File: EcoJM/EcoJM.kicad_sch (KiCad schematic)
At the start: 0 parts

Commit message: bahr updoad
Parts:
- added C1: 1n, symbol Device:C
- added C2, C4, C5: 100n, symbol Device:C
- added C3: 4.7n, symbol Device:C
- added R1: 10k, symbol Device:R
- added U1, U2: ACS712xLCTR-30A, Package_SO:SOIC-8_3.9x4.9mm_P1.27mm, symbol Sensor_Current:ACS712xLCTR-30A
- added U3: SIT65HVD230DR, EasyEDA:SOP-8_L4.9-W3.9-P1.27-LS6.0-BL, symbol EasyEDA:SIT65HVD230DR
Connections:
- new net: R1.1, U3.8 (RS)
- new net: C1.1, U1.6 (FILTER)
- new net: C3.1, U2.6 (FILTER)
- new net: U2.1 (IP+), U2.2 (IP+)
- new net: U2.3 (IP-), U2.4 (IP-)
- new net: U1.1 (IP+), U1.2 (IP+)
- new net: U1.3 (IP-), U1.4 (IP-)
- new net +3.3V: C5.2, U3.3 (VCC)
- new net +5V: C2.2, C4.2, U1.8 (VCC), U2.8 (VCC)
- new net GND: C1.2, C2.1, C3.2, C4.1, C5.1, R1.2, U1.5 (GND), U2.5 (GND), U3.2 (GND)

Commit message: Signed-off-by: Omar-Magdy0 <omar.magdy.om.om@gmail.com> Major Updates
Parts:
- removed U2: ACS712xLCTR-30A, Package_SO:SOIC-8_3.9x4.9mm_P1.27mm, symbol Sensor_Current:ACS712xLCTR-30A
- added C6: 22n, symbol Device:C
- added C7: 10u, symbol Device:C
- added F1: Fuse, Fuse:Fuseholder_Clip-5x20mm_Keystone_3512_Inline_P23.62x7.27mm_D1.02x1.57mm_Horizontal, symbol Device:Fuse
- added J1, J2: Screw_Terminal_01x02, symbol Connector:Screw_Terminal_01x02
- added J3, J4, J6: Conn_01x02_Pin, symbol Connector:Conn_01x02_Pin
- added J5, J7: Conn_01x03_Pin, symbol Connector:Conn_01x03_Pin
- added L1: 10u, symbol Device:L
- added R2, R6: 10k, symbol Device:R
- added R3, R4: R, symbol Device:R
- added R5: 120, symbol Device:R
- added R7: 20k, symbol Device:R
- added U2: MT2492, EasyEDA:SOT-23-6_L2.9-W1.6-P0.95-LS2.8-BL_3, symbol EasyEDA:MT2492
- added U4: AZ1117-3.3, Package_TO_SOT_SMD:SOT-89-3_Handsoldering, symbol Regulator_Linear:AZ1117-3.3
- added U5: RS321BXF, EasyEDA:SOT-23-5_L2.9-W1.6-P0.95-LS2.8-BL, symbol EasyEDA:RS321BXF
- C1: value 1n -> 4.7n
- C3: value 4.7n -> 22u
- C4: value 100n -> 22u
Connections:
- net +3.3V: now also C7.1, U4.2 (VO)
- net +5V: now also C3.2, L1.2, R3.1, U4.3 (VI); no longer C4.2
- net GND: now also C3.1, C4.2, C7.2, J3.2 (Pin_2), J4.2 (Pin_2), J5.3 (Pin_3), J7.3 (Pin_3), R4.2, R7.2, U2.2 (GND), U4.1 (GND); no longer C3.2, C4.1
- net CAN_TXD: now reaches U3.1 (D)
- net CAN_RXD: now reaches U3.4 (R)
- net CAN_L: now reaches U3.6 (CANL)
- net CAN_L: now also J5.2 (Pin_2), J6.2 (Pin_2)
- net CAN_H: now reaches U3.7 (CANH)
- net CAN_H: now also J5.1 (Pin_1), R5.1
- net at U1.1 (IP+), U1.2 (IP+): now also F1.2
- net VDCH+_OUT: now reaches U1.3 (IP-), U1.4 (IP-)
- net VDCH+_OUT: now also J2.1 (Pin_1)
- net at U1.7 (VIOUT): now also R6.1
- new net: C6.2, L1.1, U2.6 (SW)
- new net: J6.1 (Pin_1), R5.2
- new net: J4.1 (Pin_1), R2.1, U2.4 (EN)
- new net: R3.2, R4.1, U2.3 (FB)
- new net: C6.1, U2.1 (BS)
- new net +12V: C4.1, J3.1 (Pin_1), R2.2, U2.5 (IN)
- new net Current_M: R6.2, R7.1
- new net UART_RX: J7.2 (Pin_2)
- new net UART_TX: J7.1 (Pin_1)
- new net VDCH+_IN: F1.1, J1.1 (Pin_1)
- new net VDCH-: J1.2 (Pin_2), J2.2 (Pin_2)
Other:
- moved on the sheet: C1, C2, C5, R1, U1, U3

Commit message: sry forgot to save schematic xD
sry forgot to save schematic xD
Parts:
- added U6: STM32F_dev, symbol STM32F_devboard:STM32F_Bluepill
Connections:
- net CAN_RXD: now also U6.16 (B8)
- net CAN_TXD: now also U6.17 (B9)
- net UART_RX: now also U6.15 (B7)
- net UART_TX: now also U6.14 (B6)
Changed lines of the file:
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@@
 	(wire
 		(pts
+			(xy 27.94 97.79) (xy 36.83 97.79)
+		)
+		(stroke
+			(width 0)
+			(type default)
+		)
+	)
+	(wire
+		(pts
 			(xy 152.4 27.94) (xy 152.4 25.4)
 		)
@@
 	(wire
 		(pts
+			(xy 27.94 93.98) (xy 36.83 93.98)
+		)
+		(stroke
+			(width 0)
+			(type default)
+		)
+	)
+	(wire
+		(pts
 			(xy 147.32 166.37) (xy 147.32 170.18)
 		)
@@
 	(wire
 		(pts
+			(xy 27.94 101.6) (xy 36.83 101.6)
+		)
+		(stroke
+			(width 0)
+			(type default)
+		)
+	)
+	(wire
+		(pts
 			(xy 134.62 177.8) (xy 134.62 180.34)
 		)
@@
 	(wire
 		(pts
+			(xy 27.94 105.41) (xy 36.83 105.41)
+		)
+		(stroke
+			(width 0)
+			(type default)
+		)
+	)
+	(wire
+		(pts
 			(xy 63.5 170.18) (xy 60.96 170.18)
 		)
@@
 		)
 	)
+	(label "CAN_RXD"
+		(at 27.94 101.6 0)
+		(effects
+			(font
+				(size 1.27 1.27)
+			)
+			(justify left bottom)
+		)
+	)
 	(label "VDCH-"
 		(at 231.14 135.89 180)
@@
 		)
 	)
+	(label "CAN_TXD"
+		(at 27.94 105.41 0)
+		(effects
+			(font
+				(size 1.27 1.27)
+			)
+			(justify left bottom)
+		)
+	)
+	(label "UART_RX"
+		(at 27.94 97.79 180)
+		(effects
+			(font
+				(size 1.27 1.27)
+			)
+			(justify right bottom)
+		)
+	)
+	(label "UART_TX"
+		(at 27.94 93.98 180)
+		(effects
+			(font
+				(size 1.27 1.27)
+			)
+			(justify right bottom)
+		)
+	)
 	(symbol
 		(lib_id "power:GND")
@@
 	)
 	(symbol
+		(lib_id "STM32F_devboard:STM32F_Bluepill")
+		(at 54.61 50.8 0)
+		(unit 1)
+		(exclude_from_sim no)
+		(in_bom yes)
+		(on_board yes)
+		(dnp no)
+		(fields_autoplaced yes)
+		(property "Reference" "U6"
+			(at 54.61 38.1 0)
+			(effects
+				(font
+					(size 1.27 1.27)
+				)
+			)
+		)
+		(property "Value" "STM32F_dev"
+			(at 54.61 40.64 0)
+			(effects
+				(font
+					(size 1.27 1.27)
+				)
+			)
+		)
+		(property "Footprint" ""
+			(at 54.61 50.8 0)
+			(effects
+				(font
+					(size 1.27 1.27)
+				)
+				(hide yes)
+			)
+		)
+		(property "Datasheet" ""
+			(at 54.61 50.8 0)
+			(effects
+				(font
+					(size 1.27 1.27)
+				)
+				(hide yes)
+			)
+		)
+		(property "Description" ""
+			(at 54.61 50.8 0)
+			(effects
+				(font
+					(size 1.27 1.27)
+				)
+				(hide yes)
+			)
+		)
+		(pin "14"
+		)
+		(pin "25"
+		)
+		(pin "1"
+		)
+		(pin "11"
+		)
+		(pin "15"
+		)
+		(pin "17"
+		)
+		(pin "19"
+		)
+		(pin "12"
+		)
+		(pin "24"
+		)
+		(pin "13"
+		)
+		(pin "18"
+		)
+		(pin "3"
+		)
+		(pin "20"
+		)
+		(pin "21"
+		)
+		(pin "39"
+		)
+		(pin "4"
+		)
+		(pin "6"
+		)
+		(pin "5"
+		)
+		(pin "7"
+		)
+		(pin "8"
+		)
+		(pin "2"
+		)
+		(pin "9"
+		)
+		(pin "10"
+		)
+		(pin "16"
+		)
+		(pin "22"
+		)
+		(pin "23"
+		)
+		(pin "27"
+		)
+		(pin "28"
+		)
+		(pin "29"
+		)
+		(pin "30"
+		)
+		(pin "26"
+		)
+		(pin "31"
+		)
+		(pin "33"
+		)
+		(pin "34"
+		)
+		(pin "35"
+		)
+		(pin "36"
+		)
+		(pin "32"
+		)
+		(pin "37"
+		)
+		(pin "38"
+		)
+		(pin "40"
+		)
+		(instances
+			(project ""
+				(path "/762e6a0f-81bf-44a8-8385-e1d3d5492602"
+					(reference "U6")
+					(unit 1)
+				)
+			)
+		)
+	)
+	(symbol
 		(lib_id "power:GND")
 		(at 91.44 185.42 0)
@@
 		(dnp no)
 		(property "Reference" "J6"
-			(at 160.655 43.18 0)
+			(at 163.576 41.656 0)
 			(effects
 				(font

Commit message: Schematic = 100% , Footprints=100%
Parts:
- added J8, J9: Screw_Terminal_01x02, TerminalBlock_Phoenix:TerminalBlock_Phoenix_PT-1,5-2-3.5-H_1x02_P3.50mm_Horizontal, symbol Connector:Screw_Terminal_01x02
- added Q1, Q2: 2SD882_C842818, EasyEDA:SOT-89-3_L4.5-W2.5-P1.50-LS4.1-BR, symbol EasyEDA:2SD882_C842818
- added R10, R12: 2.2k, Resistor_SMD:R_1206_3216Metric_Pad1.30x1.75mm_HandSolder, symbol Device:R
- added R11, R9: 47k, Resistor_SMD:R_1206_3216Metric_Pad1.30x1.75mm_HandSolder, symbol Device:R
- added R13, R14, R15, R8: 470, Resistor_SMD:R_1206_3216Metric_Pad1.30x1.75mm_HandSolder, symbol Device:R
- added U7, U8: PC817C_C3025164, EasyEDA:OPTO-SMD-4_L4.6-W6.5-P2.54-LS10.3-TL, symbol EasyEDA:PC817C_C3025164
- C1, C2, C3, C4, C5, C6, C7: footprint (none) -> LED_SMD:LED_1206_3216Metric_Pad1.42x1.75mm_HandSolder
- J3: footprint (none) -> Connector_JST:JST_XH_B2B-XH-A_1x02_P2.50mm_Vertical
- J4, J6: footprint (none) -> Connector_PinHeader_2.54mm:PinHeader_1x02_P2.54mm_Vertical
- J5, J7: footprint (none) -> Connector_JST:JST_XH_B3B-XH-A_1x03_P2.50mm_Vertical
- L1: footprint (none) -> EasyEDA:IND-SMD_L7.2-W6.6_GPSR07X0
- R1, R2, R3, R4, R5, R6, R7: footprint (none) -> Resistor_SMD:R_1206_3216Metric_Pad1.30x1.75mm_HandSolder
- U6: footprint (none) -> dev_board:STM32F_devboard
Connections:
- net +3.3V: now also U5.5 (+V), U6.20 (3.3)
- net Current_M: now also U6.36 (A0)
- net GND: now also U5.2 (V-), U6.19 (GND), U6.21 (GND), U6.22 (GND), R12.1, U7.2, U8.2
- net VDCH+_IN: now also R11.1
- net VDCH-: now also R9.1
- net at U5.1 (+IN): now also R11.2, R12.2
- net at U5.3 (-IN): now also R10.2, R9.2
- net Voltage_M: now reaches U5.4 (OUT)
- net Voltage_M: now also U6.35 (A1), R10.1
- net SSR1: now reaches U6.27 (B1)
- net SSR1: now also R13.1
- net SSR0: now reaches U6.28 (B0)
- net SSR0: now also R8.1
- new net: R13.2, U8.1
- new net: R14.1, U8.3
- new net: J8.1 (Pin_1), Q1.2 (C), U8.4
- new net: J9.1 (Pin_1), Q2.2 (C), U7.4
- new net: J9.2 (Pin_2), Q2.3 (E)
- new net: Q1.1 (B), R14.2
- new net: R8.2, U7.1
- new net: R15.1, U7.3
- new net: Q2.1 (B), R15.2
- new net: J8.2 (Pin_2), Q1.3 (E)
- no-connect marks 0 -> 29
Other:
- moved on the sheet: C5, J5, J6, J7, R1, R5, U3, U5, U6

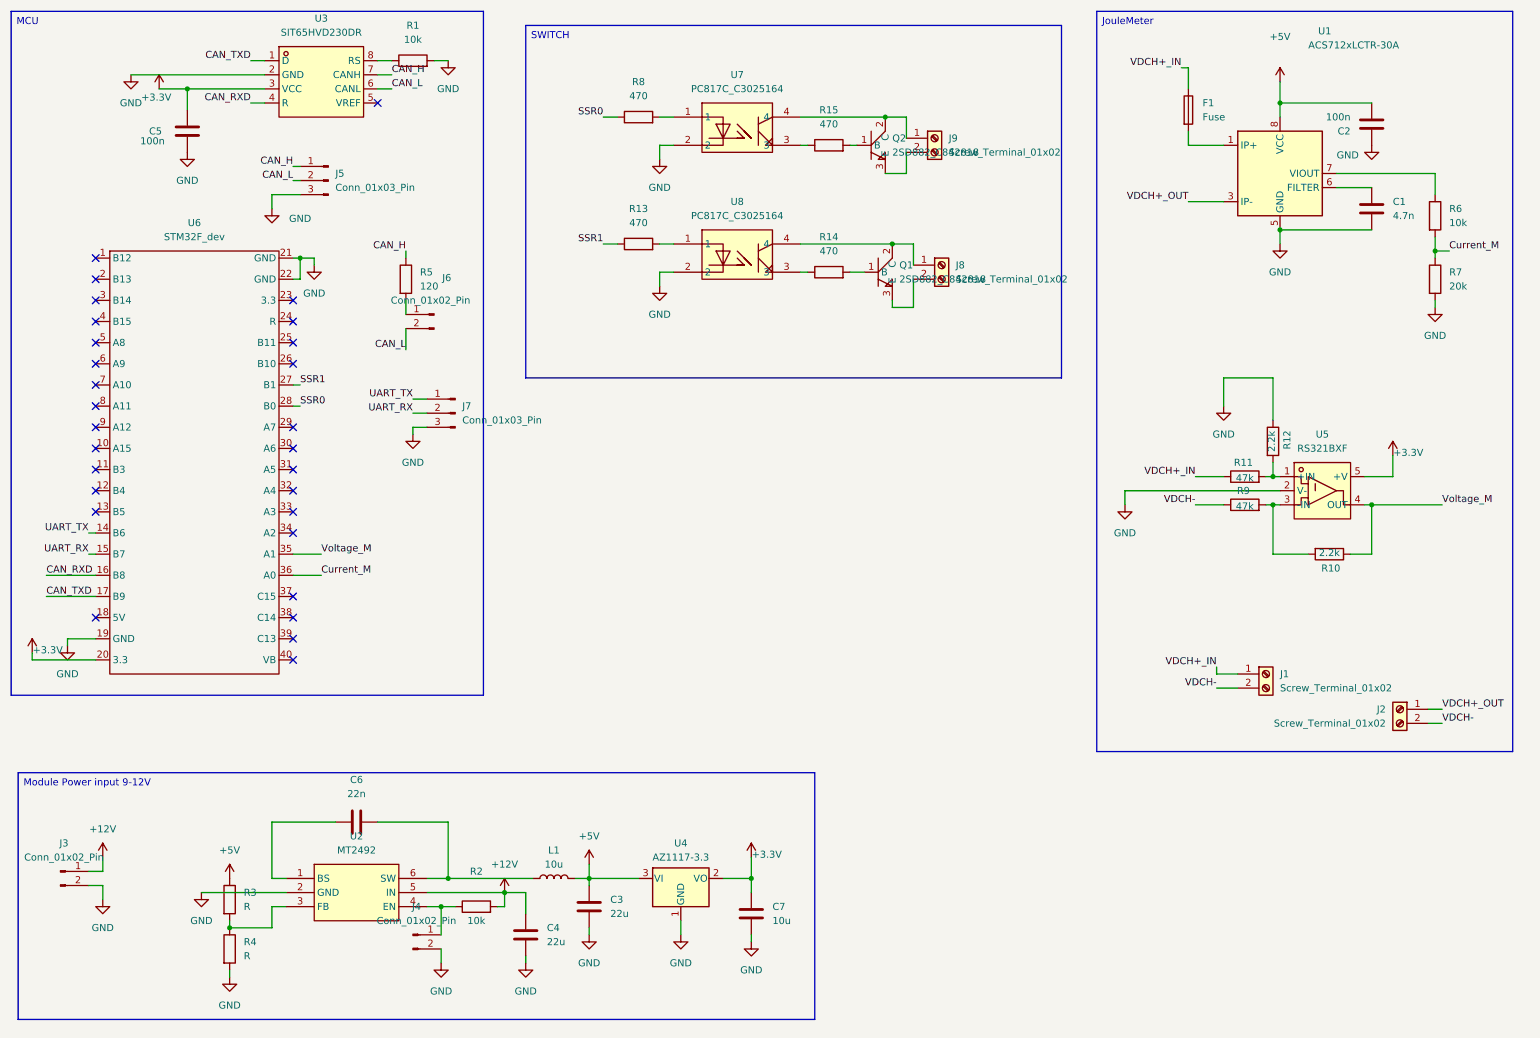
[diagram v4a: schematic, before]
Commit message: Updates
R variable added to op amp

Buck converter V division Resistors values added
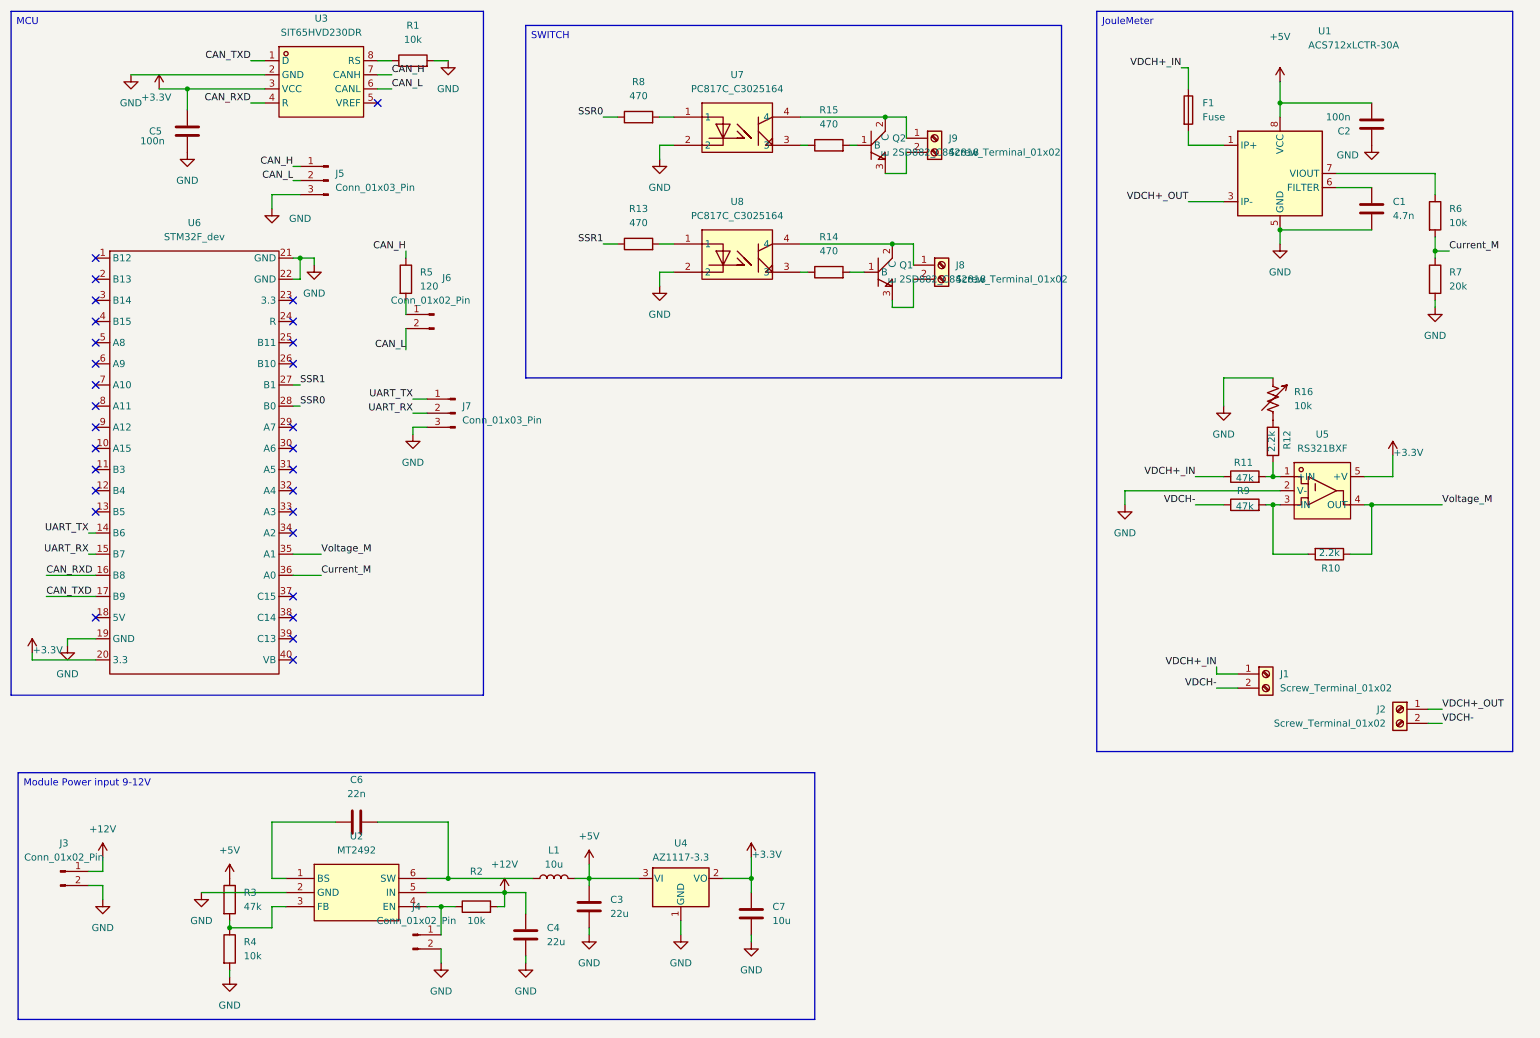
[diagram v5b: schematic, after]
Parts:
- added R16: 10k, symbol Device:R_Variable_US
- R3: value R -> 47k
- R4: value R -> 10k
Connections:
- net GND: now also R16.1; no longer R12.1
- new net: R12.1, R16.2
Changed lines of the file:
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@@
 	(wire
 		(pts
-			(xy 241.3 80.01) (xy 241.3 87.63)
-		)
-		(stroke
-			(width 0)
-			(type default)
-		)
-	)
-	(wire
-		(pts
 			(xy 60.96 49.53) (xy 60.96 46.99)
 		)
@@
 	)
 	(symbol
+		(lib_id "Device:R_Variable_US")
+		(at 241.3 83.82 0)
+		(unit 1)
+		(exclude_from_sim no)
+		(in_bom yes)
+		(on_board yes)
+		(dnp no)
+		(fields_autoplaced yes)
+		(property "Reference" "R16"
+			(at 245.11 82.5118 0)
+			(effects
+				(font
+					(size 1.27 1.27)
+				)
+				(justify left)
+			)
+		)
+		(property "Value" "10k"
+			(at 245.11 85.0518 0)
+			(effects
+				(font
+					(size 1.27 1.27)
+				)
+				(justify left)
+			)
+		)
+		(property "Footprint" ""
+			(at 239.522 83.82 90)
+			(effects
+				(font
+					(size 1.27 1.27)
+				)
+				(hide yes)
+			)
+		)
+		(property "Datasheet" "~"
+			(at 241.3 83.82 0)
+			(effects
+				(font
+					(size 1.27 1.27)
+				)
+				(hide yes)
+			)
+		)
+		(property "Description" "Variable resistor, US symbol"
+			(at 241.3 83.82 0)
+			(effects
+				(font
+					(size 1.27 1.27)
+				)
+				(hide yes)
+			)
+		)
+		(pin "1"
+		)
+		(pin "2"
+		)
+		(instances
+			(project ""
+				(path "/762e6a0f-81bf-44a8-8385-e1d3d5492602"
+					(reference "R16")
+					(unit 1)
+				)
+			)
+		)
+	)
+	(symbol
 		(lib_id "power:+5V")
 		(at 242.57 26.67 0)
@@
 			)
 		)
-		(property "Value" "R"
+		(property "Value" "10k"
 			(at 55.88 184.1499 0)
 			(effects
@@
 			)
 		)
-		(property "Value" "R"
+		(property "Value" "47k"
 			(at 55.88 175.2599 0)
 			(effects

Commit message: Schematic REV by OMAR_MAGDY , REV0 Layout 80%
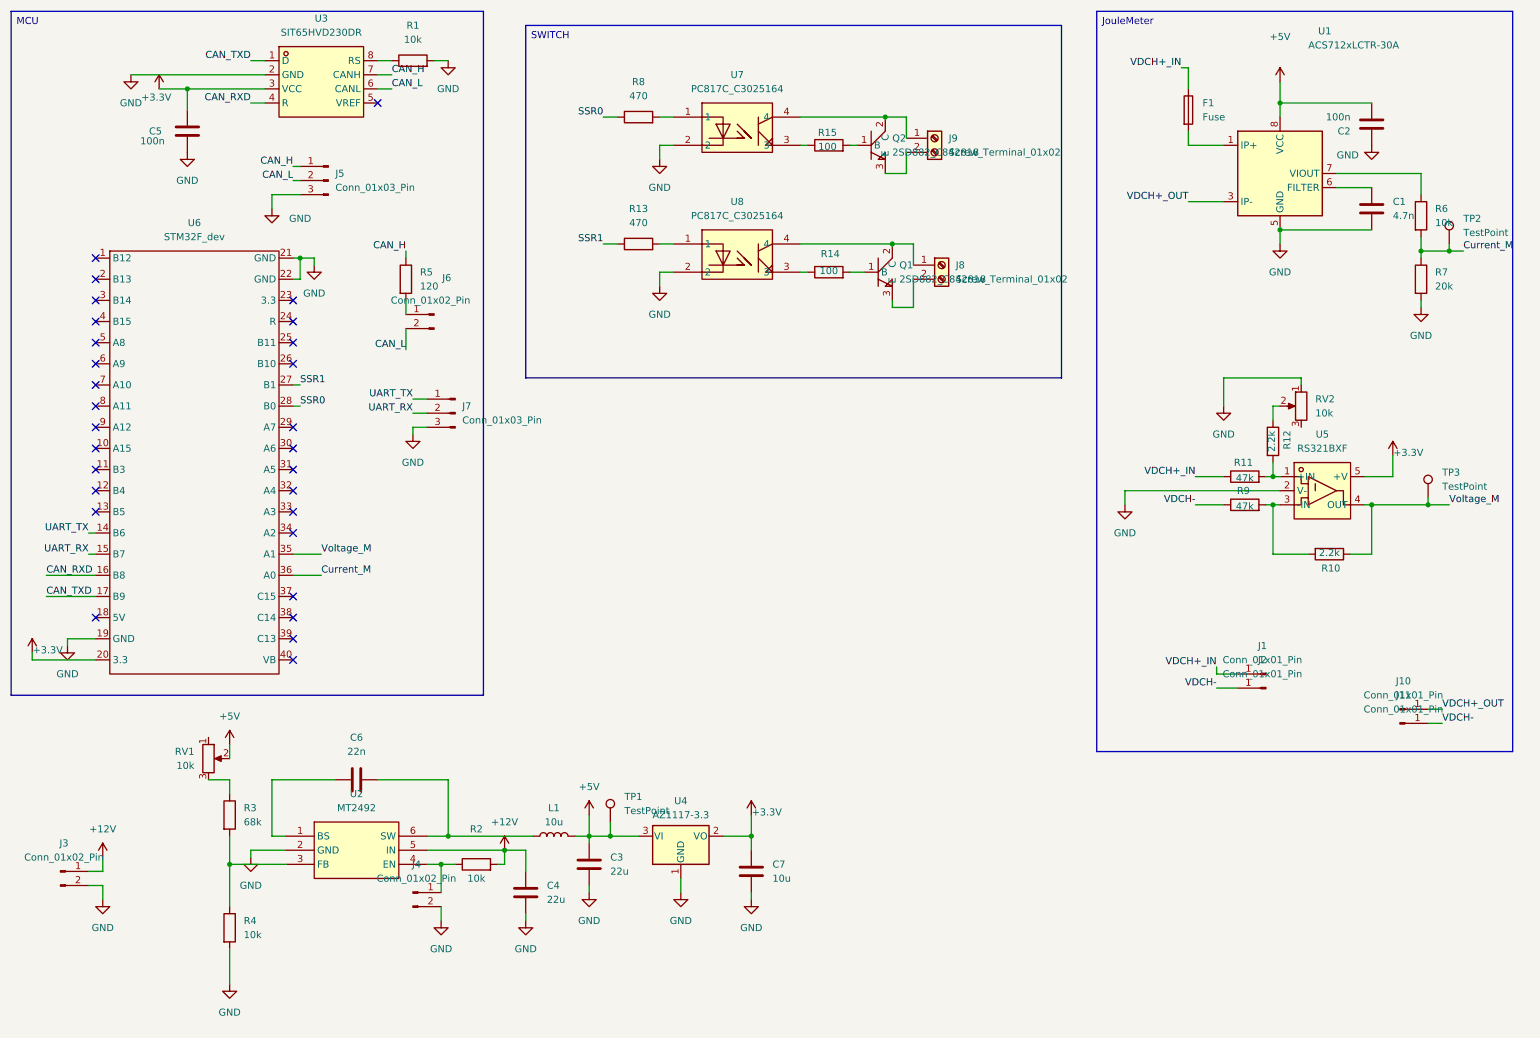
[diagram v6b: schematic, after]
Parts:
- removed J1, J2: Screw_Terminal_01x02, symbol Connector:Screw_Terminal_01x02
- removed R16: 10k, symbol Device:R_Variable_US
- added J1, J10, J11, J2: Conn_01x01_Pin, symbol Connector:Conn_01x01_Pin
- added RV1, RV2: 10k, Potentiometer_THT:Potentiometer_Bourns_3296W_Vertical, symbol Device:R_Potentiometer
- added TP1, TP2, TP3: TestPoint, TestPoint:TestPoint_Pad_D1.5mm, symbol Connector:TestPoint
- R14, R15: value 470 -> 100
- R3: value 47k -> 68k
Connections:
- net +5V: now also RV1.2, TP1.1; no longer R3.1
- net Current_M: now also TP2.1
- net GND: now also RV2.1
- net VDCH+_IN: now also J1.1 (Pin_1)
- net VDCH+_OUT: now also J10.1 (Pin_1)
- net VDCH-: now also J11.1 (Pin_1), J2.1 (Pin_1)
- net Voltage_M: now also TP3.1
- net at R12.1: now also RV2.2
- new net: R3.1, RV1.3
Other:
- moved on the sheet: C3, C4, C6, C7, J4, L1, R2, R3, R4, R6, R7, U2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
